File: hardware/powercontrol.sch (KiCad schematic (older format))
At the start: 17 parts, among them Q1 IRF9540N, Q2 IRF9540N, Q3 2N3904, SW1 SW_Push, SW2 SW_Push, U1 TL072

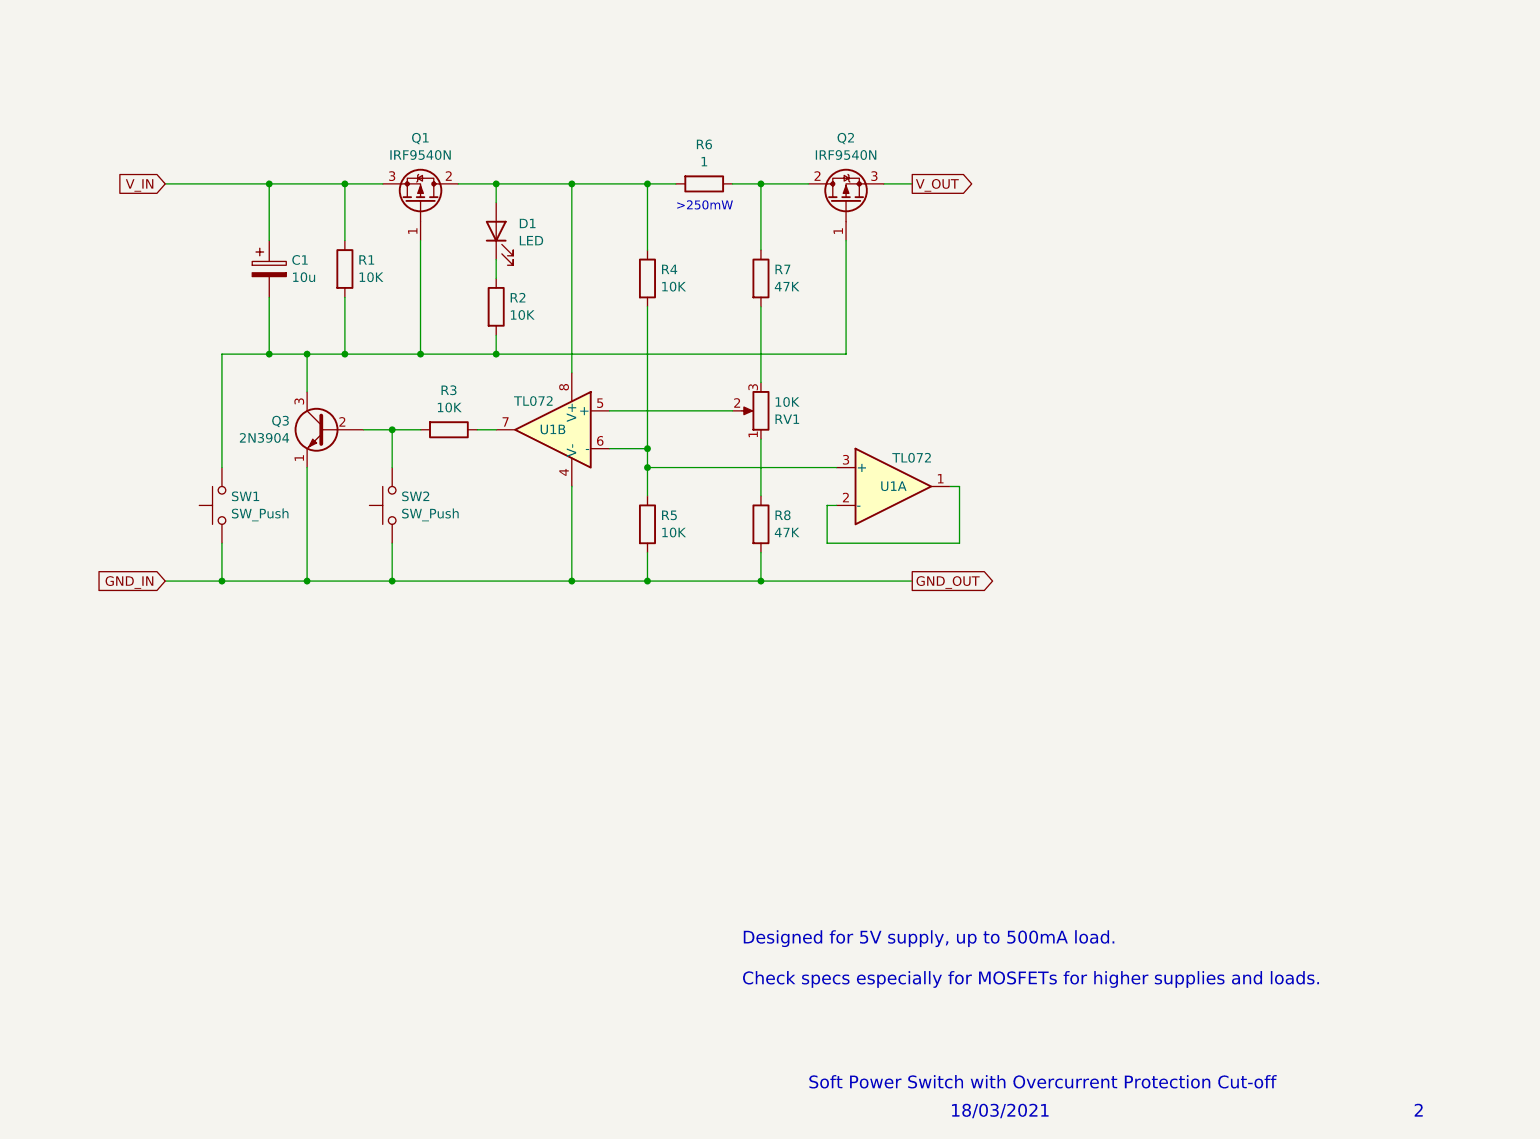
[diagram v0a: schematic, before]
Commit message: V4 - Veroboard layout fixes, actually built and tested on veroboard now
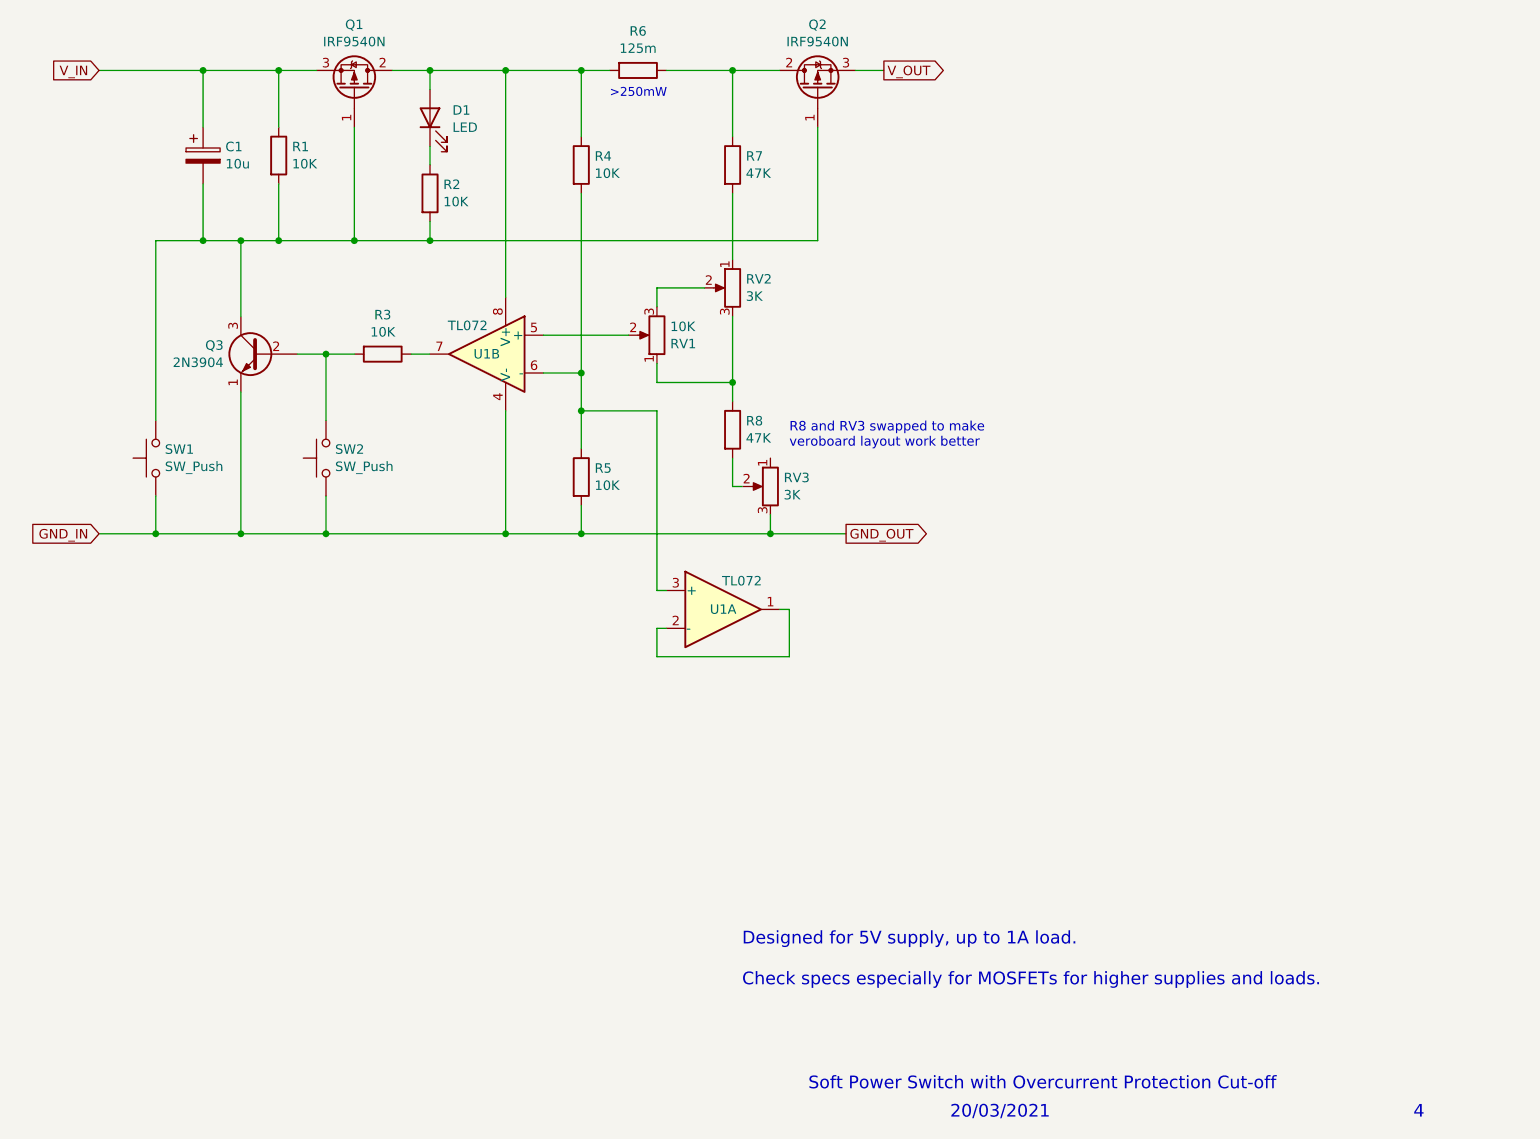
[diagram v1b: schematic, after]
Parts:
- added RV2, RV3: 3K, Potentiometer_THT:Potentiometer_Runtron_RM-065_Vertical, symbol Device:R_POT
- R6: value 1 -> 125m
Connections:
- net GND_IN: now also RV3.3; no longer R8.2
- net at R8.1, RV1.1: now also RV2.3
- net at RV1.3: now also RV2.2; no longer R7.2
- new net: R7.2, RV2.1
- new net: R8.2, RV3.2
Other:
- note added: "20/03/2021"
- note added: "4"
- note added: "Designed for 5V supply, up to 1A load.\n\nCheck specs especially for MOSFETs for higher supplies and loads."
- note added: "R8 and RV3 swapped to make\nveroboard layout work better"
- note removed: "18/03/2021"
- note removed: "2"
- note removed: "Designed for 5V supply, up to 500mA load.\n\nCheck specs especially for MOSFETs for higher supplies and loads."
- moved on the sheet: C1, D1, Q1, Q2, Q3, R1, R2, R3, R4, R5, R6, R7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

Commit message: Add images of breadboard, veroboard, schematic
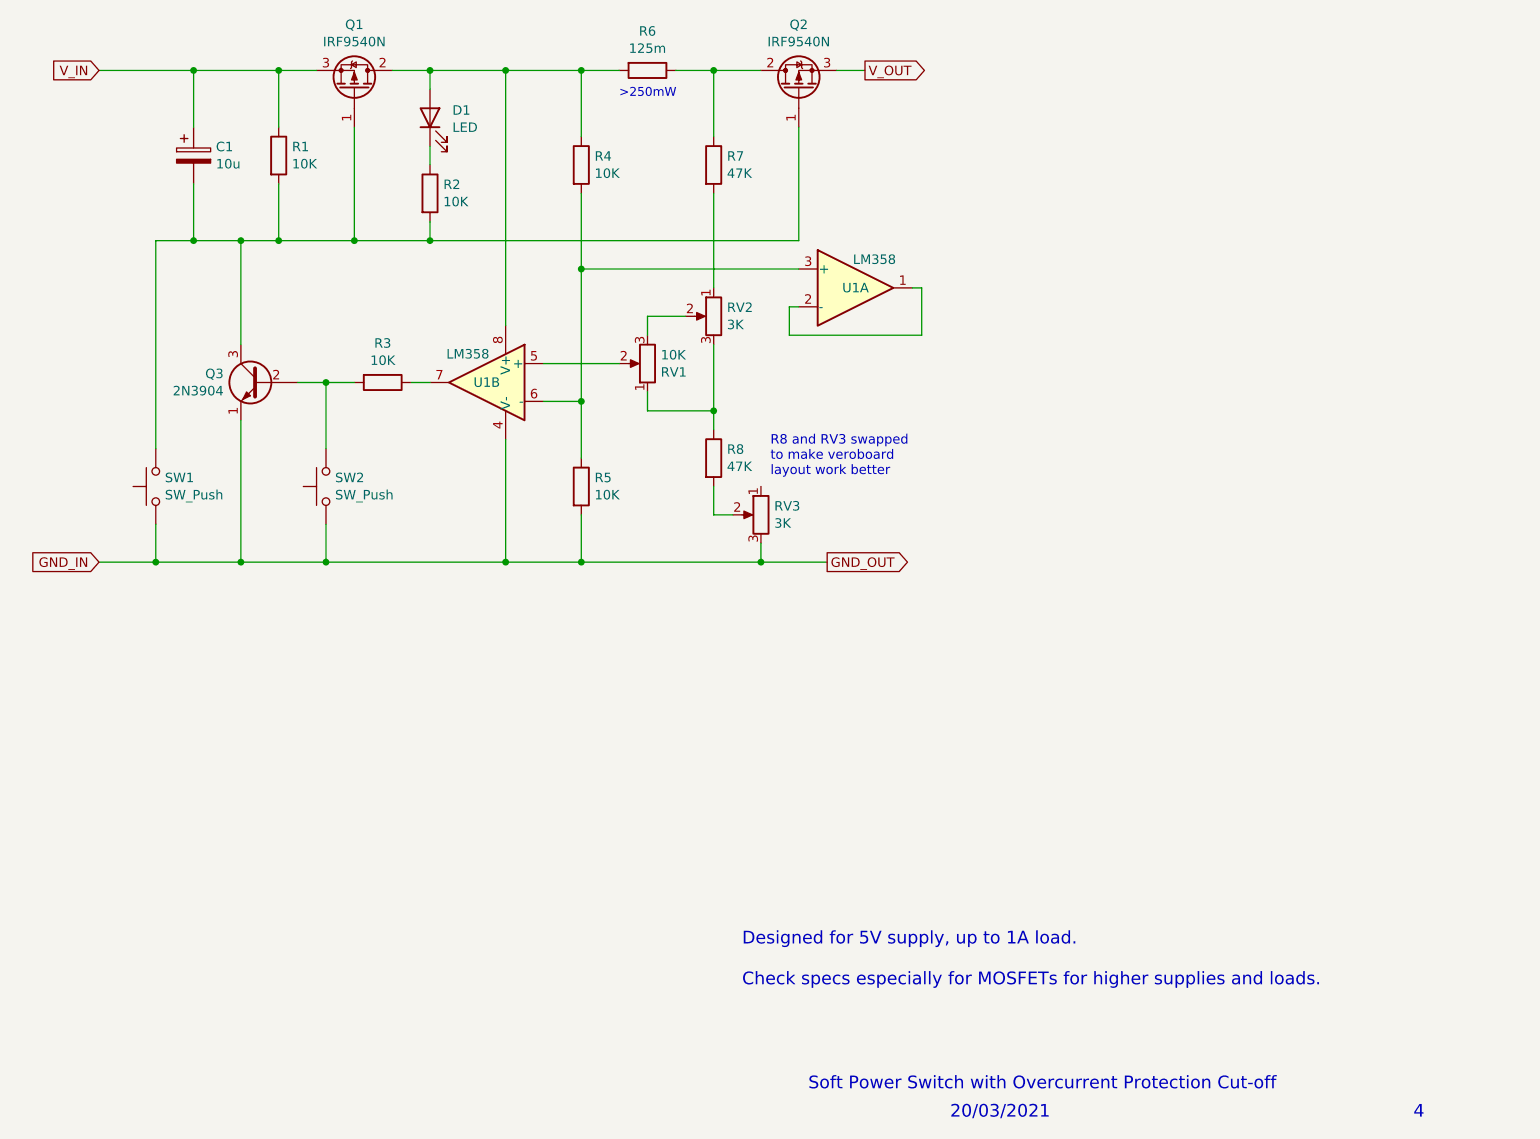
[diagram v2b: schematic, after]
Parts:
- U1: value TL072 -> LM358
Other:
- note added: "R8 and RV3 swapped \nto make veroboard \nlayout work better"
- note removed: "R8 and RV3 swapped to make\nveroboard layout work better"
- moved on the sheet: C1, Q2, Q3, R3, R5, R6, R7, R8, RV1, RV2, RV3, SW1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
